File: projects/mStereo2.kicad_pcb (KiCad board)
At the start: 4 copper layers, 159.5 x 120 mm, 125 parts, among them P101 CONN_AMANERO, P102 Screw-term 1x2, P103 Screw-term 1X3, P104 XLR-MALE, P105 XLR-MALE, U101 ISO7640, U102 CDCLVC1104, U103 MCP100-315DI, U104 SRC4192, U201 LT1761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

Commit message: final changes to top silkscreen layout
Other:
- board text added: "rev. 2.0"
- board text added: "serial no."
- board text removed: "rev. 2.00"
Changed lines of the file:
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@@
     (area 15.939714 20.852 279.041143 171.888)
     (thickness 1.6)
-    (drawings 93)
+    (drawings 103)
     (tracks 946)
     (zones 0)
@@
   )
   (layers
-    (15 F.Cu signal hide)
+    (15 F.Cu signal)
     (2 InnerF.Cu signal hide)
     (1 InnerB.Cu signal hide)
@@
     (21 F.SilkS user)
     (22 B.Mask user)
-    (23 F.Mask user)
-    (24 Dwgs.User user)
-    (25 Cmts.User user)
+    (23 F.Mask user hide)
+    (24 Dwgs.User user hide)
+    (25 Cmts.User user hide)
     (26 Eco1.User user hide)
     (27 Eco2.User user hide)
@@
     (visible_elements FFFFFF3F)
     (pcbplotparams
-      (layerselection 284196871)
+      (layerselection 2097152)
       (usegerberextensions true)
       (excludeedgelayer true)
@@
       (solder_mask_margin 0.75) (clearance 0.75))
   )
+  (gr_line (start 177.546 42.164) (end 171.704 42.164) (angle 90) (layer F.Mask) (width 0.2))
+  (gr_line (start 170.942 42.164) (end 177.546 42.164) (angle 90) (layer F.Mask) (width 0.2))
+  (gr_text "serial no." (at 179.832 39.116) (layer F.SilkS)
+    (effects (font (size 1.5 1.5) (thickness 0.2)) (justify right))
+  )
+  (gr_line (start 169.926 40.64) (end 169.926 44.196) (angle 90) (layer F.SilkS) (width 0.7))
+  (gr_line (start 178.816 40.64) (end 178.816 44.196) (angle 90) (layer F.SilkS) (width 0.7))
+  (gr_line (start 169.418 40.386) (end 169.418 44.45) (angle 90) (layer F.SilkS) (width 0.5))
+  (gr_line (start 179.324 40.386) (end 179.324 44.45) (angle 90) (layer F.SilkS) (width 0.5))
+  (gr_line (start 179.32 44.45) (end 169.418 44.45) (angle 90) (layer F.SilkS) (width 0.5))
+  (gr_line (start 169.418 40.386) (end 179.32 40.386) (angle 90) (layer F.SilkS) (width 0.5))
+  (gr_line (start 171.196 42.418) (end 177.55 42.418) (angle 90) (layer F.SilkS) (width 4))
   (gr_text "(c) Amanero SRL" (at 69.85 62.865 90) (layer F.SilkS)
     (effects (font (size 0.5 0.5) (thickness 0.1)) (justify right))
@@
     (effects (font (size 0.5 0.5) (thickness 0.1)) (justify right))
   )
-  (gr_text "rev. 2.00" (at 175.26 144.78) (layer F.SilkS)
+  (gr_text "rev. 2.0" (at 175.26 144.78) (layer F.SilkS)
     (effects (font (size 1.5 1.5) (thickness 0.2)) (justify right))
   )

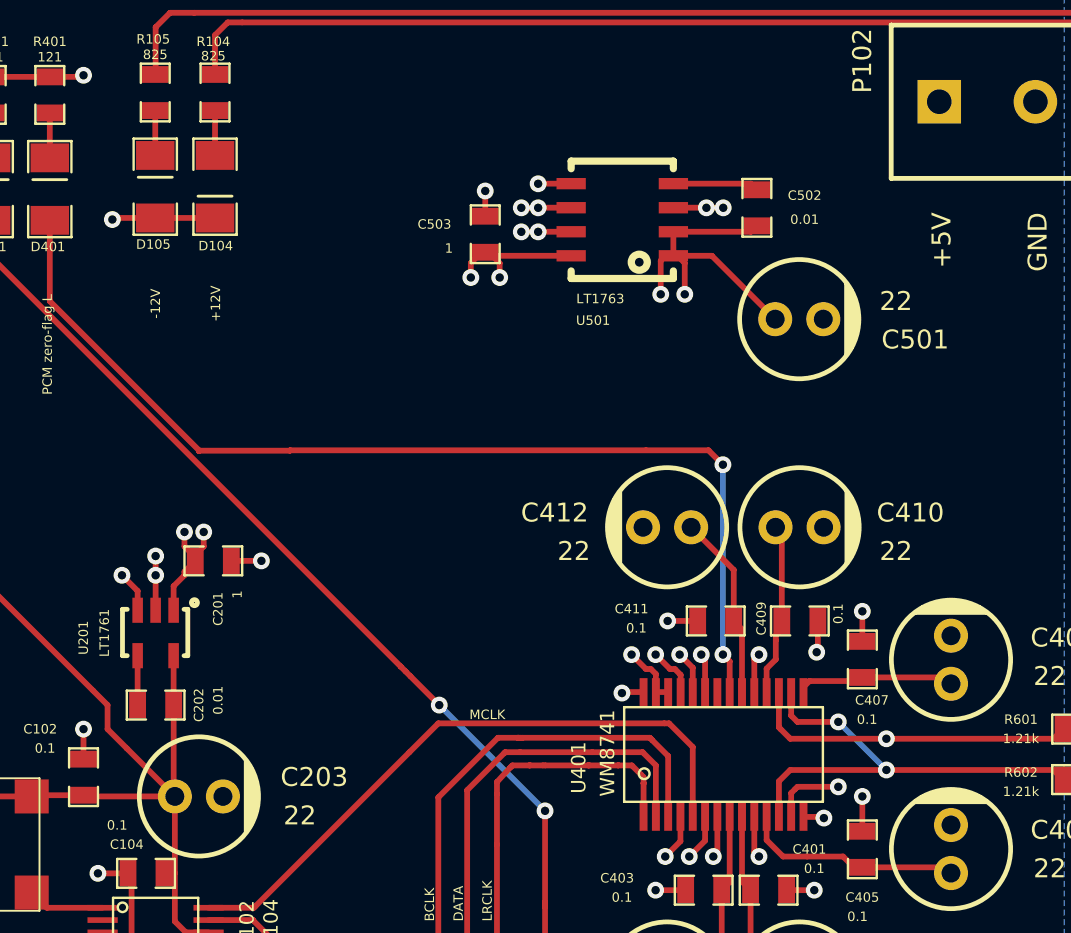
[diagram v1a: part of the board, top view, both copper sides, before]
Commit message: fix errors reported by fab (hole spacing too close; 5 places), generate new set of gerbers for resubmission
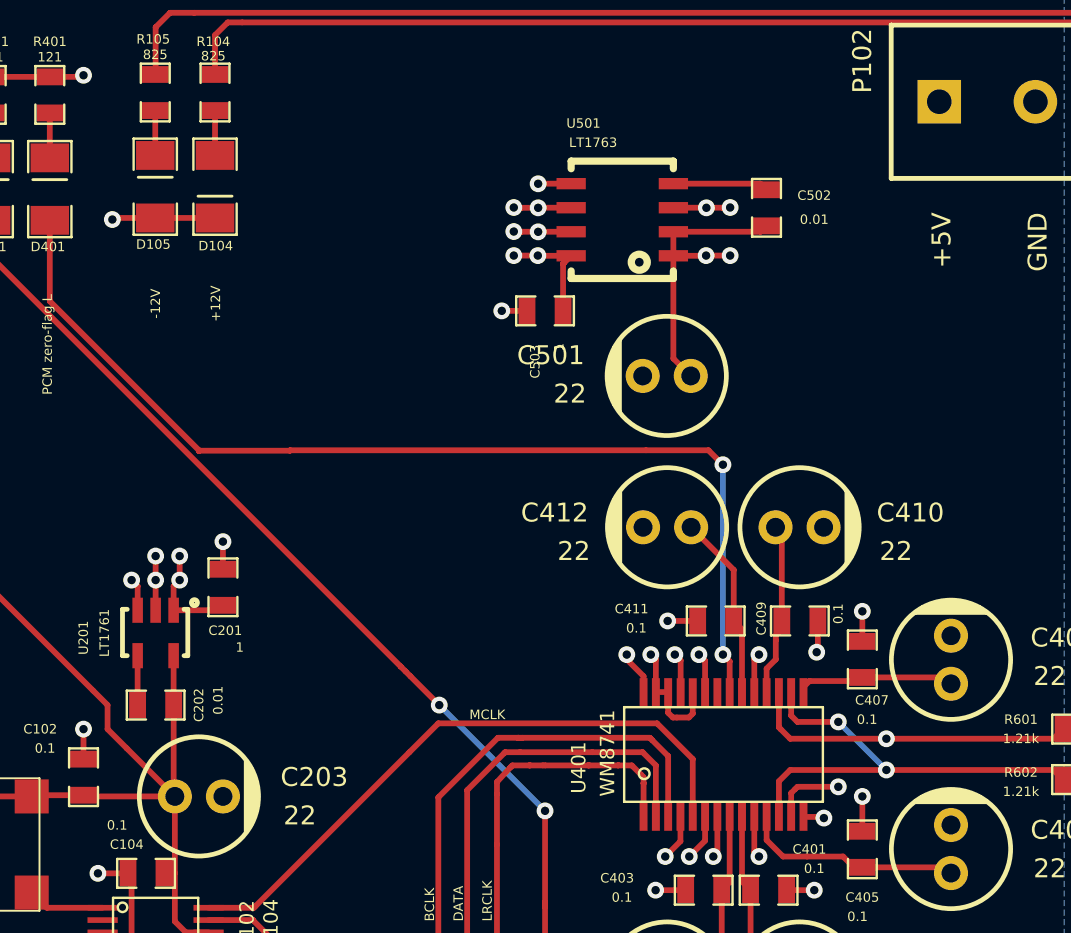
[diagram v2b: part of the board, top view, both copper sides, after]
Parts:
- moved C501 7.62 mm to (122.0, 55.0), turned to 180 degrees
- moved C503 5.13 mm to (115.6, 51.6), turned to 180 degrees
- moved C201 1.49 mm to (98.6, 66.2), turned to 90 degrees
- moved C502 0.51 mm to (127.3, 46.1)
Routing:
- net +5V: track 74.1 -> 70.9 mm
- net DGND: track 130.4 -> 132.4 mm, vias 54 -> 53
- net VDD: track 86.5 -> 85.1 mm
